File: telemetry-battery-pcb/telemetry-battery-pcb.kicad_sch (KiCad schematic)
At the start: 67 parts, among them J1 Network Connector, J3 CONN_360410_MZC, J5 CONN_360410_MZC, Q1 NMOS, Q2 PMOS, Q4 NMOS, U4 LTC2944, U5 XR76208, U6 M24C02-WMN, U7 TPS1HTC30-Q1

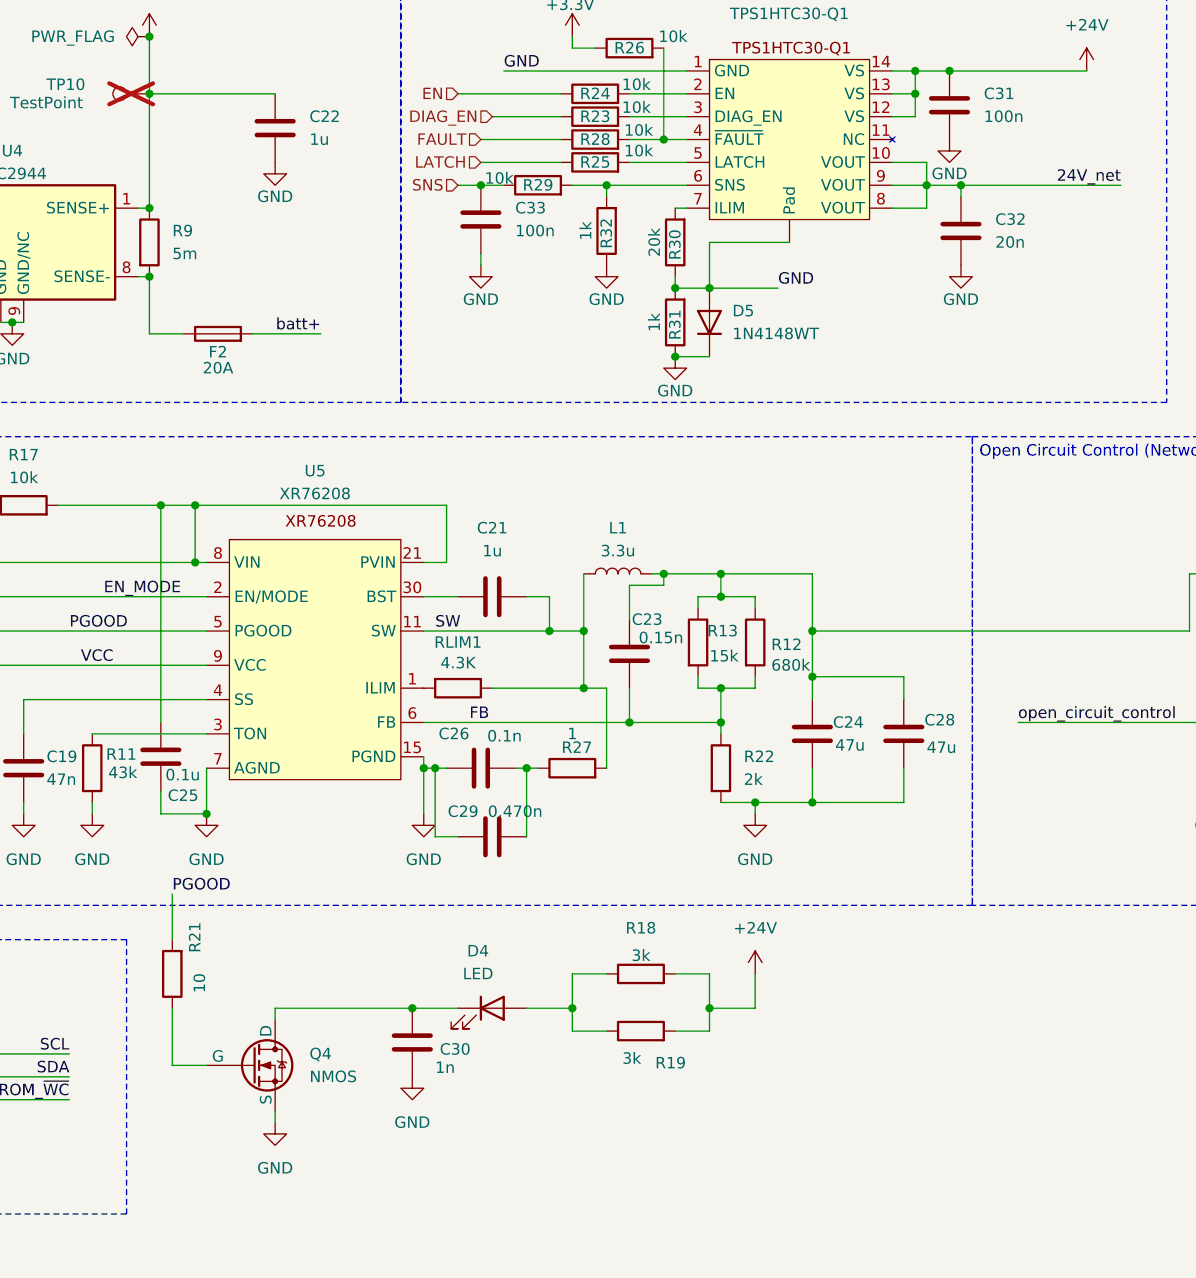
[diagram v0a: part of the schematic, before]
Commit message: telemetry-battery-pcb: schematic connections complete
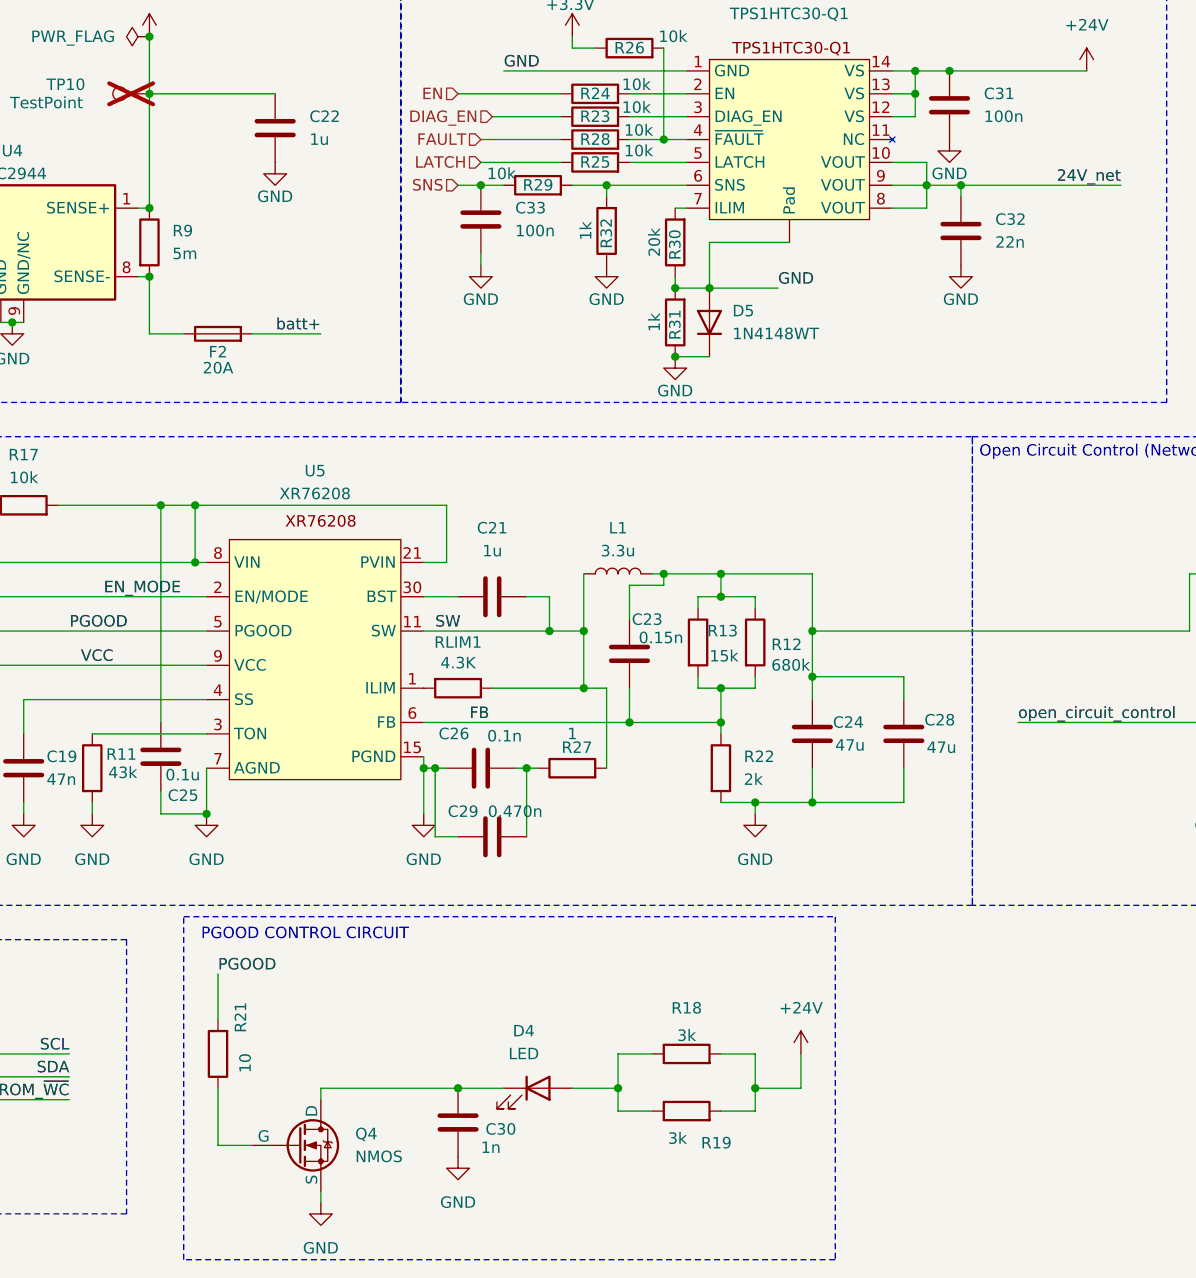
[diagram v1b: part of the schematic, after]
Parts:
- C31, C33: footprint (none) -> Capacitor_SMD:C_0402_1005Metric; JLCPCB (none) -> C1581
- C32: value 20n -> 22n; footprint (none) -> Capacitor_SMD:C_0402_1005Metric; JLCPCB (none) -> C1532
- R23, R24, R25, R26, R28, R29: footprint (none) -> Resistor_SMD:R_0402_1005Metric; JLCPCB (none) -> C25744
- R30: footprint (none) -> Resistor_SMD:R_0201_0603Metric; JLCPCB (none) -> C4184
- R31: footprint (none) -> Resistor_SMD:R_0402_1005Metric; JLCPCB (none) -> C11702
- U5: JLCPCB (none) -> C555356
- U7: footprint (none) -> Package_SO:Texas_HTSSOP-14-1EP_4.4x5mm_P0.65mm_EP3.4x5mm_Mask3.155x3.255mm_ThermalVias; JLCPCB (none) -> C22414694
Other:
- note added: "PGOOD CONTROL CIRCUIT"
- moved on the sheet: C30, D4, Q4, R18, R19, R21

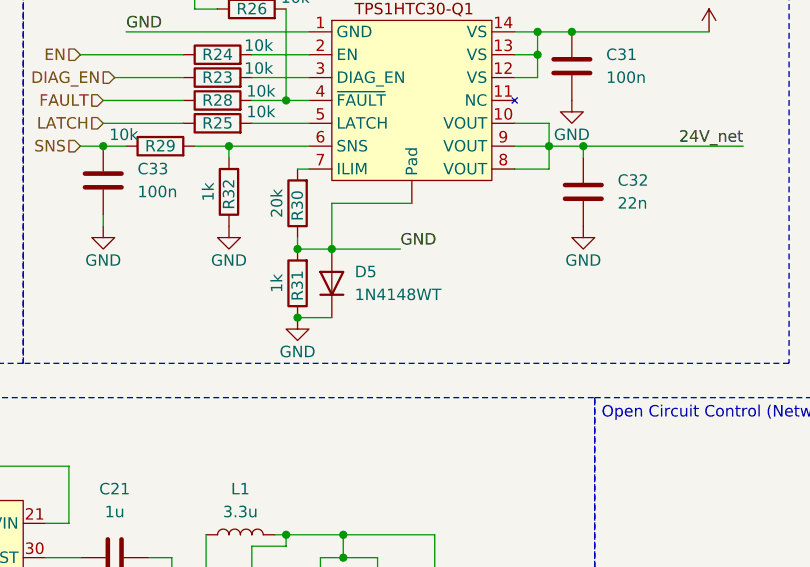
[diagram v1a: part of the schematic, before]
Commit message: telemetry_battery: modify footprint tps1htc30
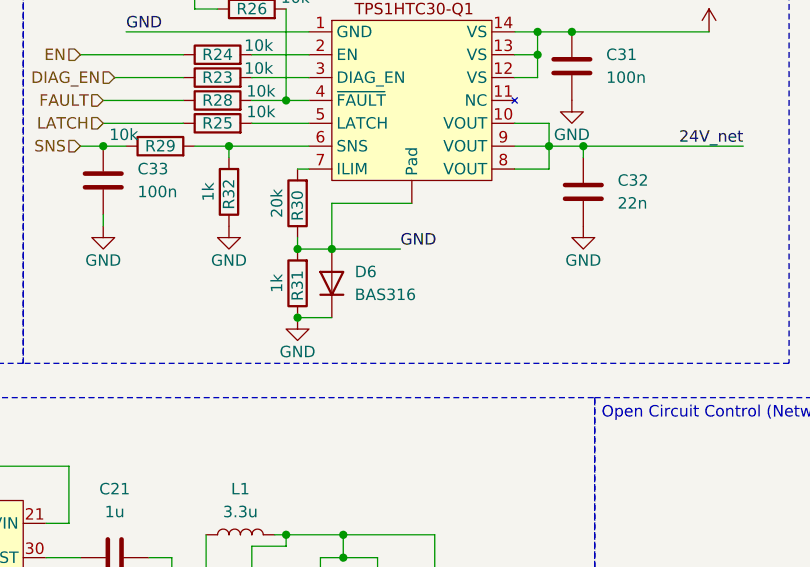
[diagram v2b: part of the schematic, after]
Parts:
- removed D5: 1N4148WT, Diode_SMD:D_SOD-523, symbol Diode:1N4148WT
- added D6: BAS316, Diode_SMD:D_SOD-323, symbol Diode:BAS316
- C31, C33: footprint Capacitor_SMD:C_0402_1005Metric -> Capacitor_SMD:C_0201_0603Metric; JLCPCB C1581 -> C14663
- U7: footprint Package_SO:Texas_HTSSOP-14-1EP_4.4x5mm_P0.65mm_EP3.4x5mm_Mask3.155x3.255mm_ThermalVias -> Exocet:Tps1htc30_Texas_HTSSOP-14-1EP_4.4x5mm_P0.65mm_EP3.4x5mm_Mask3.155x3.255mm_ThermalVias
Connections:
- net GND: now also D6.1 (K), D6.2 (A)
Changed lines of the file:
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@@
 	)
 	(symbol
-		(lib_id "Diode:1N4148WT")
-		(at 130.81 87.63 90)
-		(unit 1)
-		(exclude_from_sim no)
-		(in_bom yes)
-		(on_board yes)
-		(dnp no)
-		(fields_autoplaced yes)
-		(property "Reference" "D5"
-			(at 133.35 86.3599 90)
-			(effects
-				(font
-					(size 1.27 1.27)
-				)
-				(justify right)
-			)
-		)
-		(property "Value" "1N4148WT"
-			(at 133.35 88.8999 90)
-			(effects
-				(font
-					(size 1.27 1.27)
-				)
-				(justify right)
-			)
-		)
-		(property "Footprint" "Diode_SMD:D_SOD-523"
-			(at 135.255 87.63 0)
-			(effects
-				(font
-					(size 1.27 1.27)
-				)
-				(hide yes)
-			)
-		)
-		(property "Datasheet" "https://www.diodes.com/assets/Datasheets/ds30396.pdf"
-			(at 130.81 87.63 0)
-			(effects
-				(font
-					(size 1.27 1.27)
-				)
-				(hide yes)
-			)
-		)
-		(property "Description" "75V 0.15A Fast switching Diode, SOD-523"
-			(at 130.81 87.63 0)
-			(effects
-				(font
-					(size 1.27 1.27)
-				)
-				(hide yes)
-			)
-		)
-		(property "Sim.Device" "D"
-			(at 130.81 87.63 0)
-			(effects
-				(font
-					(size 1.27 1.27)
-				)
-				(hide yes)
-			)
-		)
-		(property "Sim.Pins" "1=K 2=A"
-			(at 130.81 87.63 0)
-			(effects
-				(font
-					(size 1.27 1.27)
-				)
-				(hide yes)
-			)
-		)
-		(pin "2"
-		)
-		(pin "1"
-		)
-		(instances
-			(project ""
-				(path "/4b4cf3aa-c94c-4150-b9c5-35049cd71136"
-					(reference "D5")
-					(unit 1)
-				)
-			)
-		)
-	)
-	(symbol
 		(lib_id "power:GND")
 		(at 158.75 81.28 0)
@@
 	)
 	(symbol
+		(lib_id "Diode:BAS316")
+		(at 130.81 87.63 90)
+		(unit 1)
+		(exclude_from_sim no)
+		(in_bom yes)
+		(on_board yes)
+		(dnp no)
+		(fields_autoplaced yes)
+		(property "Reference" "D6"
+			(at 133.35 86.3599 90)
+			(effects
+				(font
+					(size 1.27 1.27)
+				)
+				(justify right)
+			)
+		)
+		(property "Value" "BAS316"
+			(at 133.35 88.8999 90)
+			(effects
+				(font
+					(size 1.27 1.27)
+				)
+				(justify right)
+			)
+		)
+		(property "Footprint" "Diode_SMD:D_SOD-323"
+			(at 135.255 87.63 0)
+			(effects
+				(font
+					(size 1.27 1.27)
+				)
+				(hide yes)
+			)
+		)
+		(property "Datasheet" "https://assets.nexperia.com/documents/data-sheet/BAS16_SER.pdf"
+			(at 130.81 87.63 0)
+			(effects
+				(font
+					(size 1.27 1.27)
+				)
+				(hide yes)
+			)
+		)
+		(property "Description" "100V, 0.25A, High-speed Switching Diode, SOD-323"
+			(at 130.81 87.63 0)
+			(effects
+				(font
+					(size 1.27 1.27)
+				)
+				(hide yes)
+			)
+		)
+		(property "Sim.Device" "D"
+			(at 130.81 87.63 0)
+			(effects
+				(font
+					(size 1.27 1.27)
+				)
+				(hide yes)
+			)
+		)
+		(property "Sim.Pins" "1=K 2=A"
+			(at 130.81 87.63 0)
+			(effects
+				(font
+					(size 1.27 1.27)
+				)
+				(hide yes)
+			)
+		)
+		(property "JLCPCB" "C2128"
+			(at 130.81 87.63 90)
+			(effects
+				(font
+					(size 1.27 1.27)
+				)
+				(hide yes)
+			)
+		)
+		(pin "1"
+		)
+		(pin "2"
+		)
+		(instances
+			(project ""
+				(path "/4b4cf3aa-c94c-4150-b9c5-35049cd71136"
+					(reference "D6")
+					(unit 1)
+				)
+			)
+		)
+	)
+	(symbol
 		(lib_id "Device:R")
 		(at 118.11 67.31 90)
@@
 			)
 		)
-		(property "Footprint" "Package_SO:Texas_HTSSOP-14-1EP_4.4x5mm_P0.65mm_EP3.4x5mm_Mask3.155x3.255mm_ThermalVias"
+		(property "Footprint" "Exocet:Tps1htc30_Texas_HTSSOP-14-1EP_4.4x5mm_P0.65mm_EP3.4x5mm_Mask3.155x3.255mm_ThermalVias"
 			(at 139.7 53.34 0)
 			(effects
@@
 			)
 		)
-		(property "Datasheet" "https://jlcpcb.com/partdetail/24038323-TPS1HTC30AQPWPRQ1/C22414694"
+		(property "Datasheet" "https://www.ti.com/lit/ds/symlink/tps1htc30-q1.pdf?ts=1772309406015"
 			(at 139.7 53.34 0)
 			(effects
@@
 			)
 		)
-		(property "Footprint" "Capacitor_SMD:C_0402_1005Metric"
+		(property "Footprint" "Capacitor_SMD:C_0201_0603Metric"
 			(at 158.4452 67.31 0)
 			(effects
@@
 			)
 		)
-		(property "JLCPCB" "C1581"
+		(property "JLCPCB" "C14663"
 			(at 157.48 63.5 0)
 			(effects
@@
 			)
 		)
-		(property "Footprint" "Capacitor_SMD:C_0402_1005Metric"
+		(property "Footprint" "Capacitor_SMD:C_0201_0603Metric"
 			(at 106.3752 80.01 0)
 			(effects
@@
 			)
 		)
-		(property "JLCPCB" "C1581"
+		(property "JLCPCB" "C14663"
 			(at 105.41 76.2 0)
 			(effects

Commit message: telemetry battery: move footprint XR76208 to Exocet Library
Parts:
- R32: footprint (none) -> Resistor_SMD:R_0402_1005Metric; JLCPCB (none) -> C11702
- U5: footprint DC-DC_XR76208ELTR-F:MaxLinear_XR76208ELTR-F_QFN-30(5x5) -> Exocet:MaxLinear_XR76208ELTR-F_QFN-30(5x5)
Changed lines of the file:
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@@
 			)
 		)
-		(property "Footprint" ""
+		(property "Footprint" "Resistor_SMD:R_0402_1005Metric"
 			(at 121.158 77.47 90)
 			(effects
@@
 		(property "Description" "Resistor"
 			(at 119.38 77.47 0)
+			(effects
+				(font
+					(size 1.27 1.27)
+				)
+				(hide yes)
+			)
+		)
+		(property "JLCPCB" "C11702"
+			(at 119.38 77.47 90)
 			(effects
 				(font
@@
 			)
 		)
-		(property "Footprint" "DC-DC_XR76208ELTR-F:MaxLinear_XR76208ELTR-F_QFN-30(5x5)"
+		(property "Footprint" "Exocet:MaxLinear_XR76208ELTR-F_QFN-30(5x5)"
 			(at 87.63 105.41 0)
 			(effects

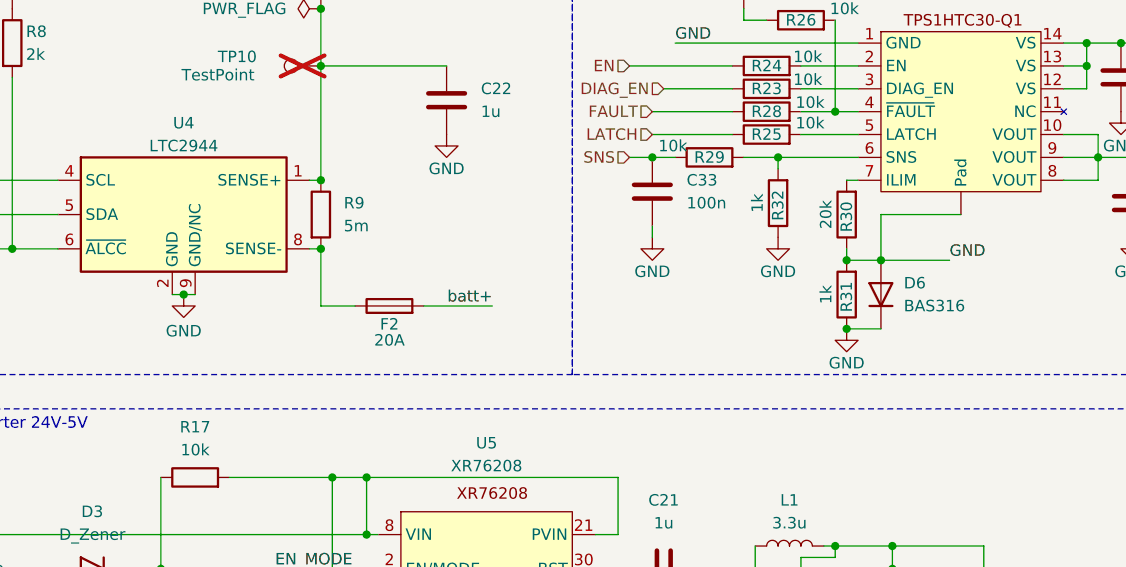
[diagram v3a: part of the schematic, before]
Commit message: telemetry-battery: start of routing
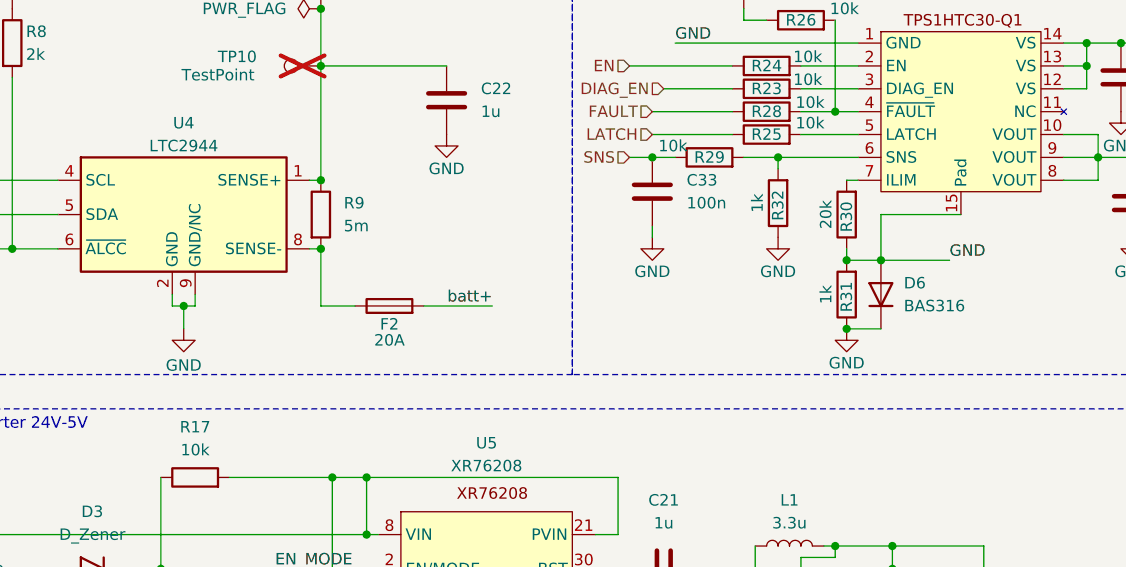
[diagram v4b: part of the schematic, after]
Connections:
- net GND: now also U7.15 (Pad); no longer U7. (Pad)
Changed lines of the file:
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@@
 	)
 	(junction
-		(at 53.34 87.63)
+		(at 53.34 88.9)
 		(diameter 0)
 		(color 0 0 0 0)
@@
 	(wire
 		(pts
-			(xy 52.07 87.63) (xy 53.34 87.63)
+			(xy 52.07 88.9) (xy 53.34 88.9)
 		)
 		(stroke
@@
 	(wire
 		(pts
+			(xy 52.07 88.9) (xy 52.07 87.63)
+		)
+		(stroke
+			(width 0)
+			(type default)
+		)
+	)
+	(wire
+		(pts
 			(xy 115.57 72.39) (xy 119.38 72.39)
 		)
@@
 	(wire
 		(pts
-			(xy 53.34 87.63) (xy 54.61 87.63)
+			(xy 53.34 88.9) (xy 54.61 88.9)
 		)
 		(stroke
@@
 	(wire
 		(pts
+			(xy 54.61 88.9) (xy 54.61 87.63)
+		)
+		(stroke
+			(width 0)
+			(type default)
+		)
+	)
+	(wire
+		(pts
 			(xy 186.69 34.29) (xy 187.96 34.29)
 		)
@@
 	(wire
 		(pts
+			(xy 53.34 91.44) (xy 53.34 88.9)
+		)
+		(stroke
+			(width 0)
+			(type default)
+		)
+	)
+	(wire
+		(pts
 			(xy 73.66 114.3) (xy 74.93 114.3)
 		)
@@
 	(symbol
 		(lib_id "power:GND")
-		(at 53.34 87.63 0)
+		(at 53.34 91.44 0)
 		(unit 1)
 		(exclude_from_sim no)
@@
 		(dnp no)
 		(property "Reference" "#PWR035"
-			(at 53.34 93.98 0)
+			(at 53.34 97.79 0)
 			(effects
 				(font
@@
 		)
 		(property "Value" "GND"
-			(at 53.34 91.694 0)
+			(at 53.34 95.504 0)
 			(effects
 				(font
@@
 		)
 		(property "Footprint" ""
-			(at 53.34 87.63 0)
+			(at 53.34 91.44 0)
 			(effects
 				(font
@@
 		)
 		(property "Datasheet" ""
-			(at 53.34 87.63 0)
+			(at 53.34 91.44 0)
 			(effects
 				(font
@@
 		)
 		(property "Description" "Power symbol creates a global label with name \"GND\" , ground"
-			(at 53.34 87.63 0)
+			(at 53.34 91.44 0)
 			(effects
 				(font
@@
 		(pin "6"
 		)
-		(pin ""
+		(pin "15"
 		)
 		(pin "14"

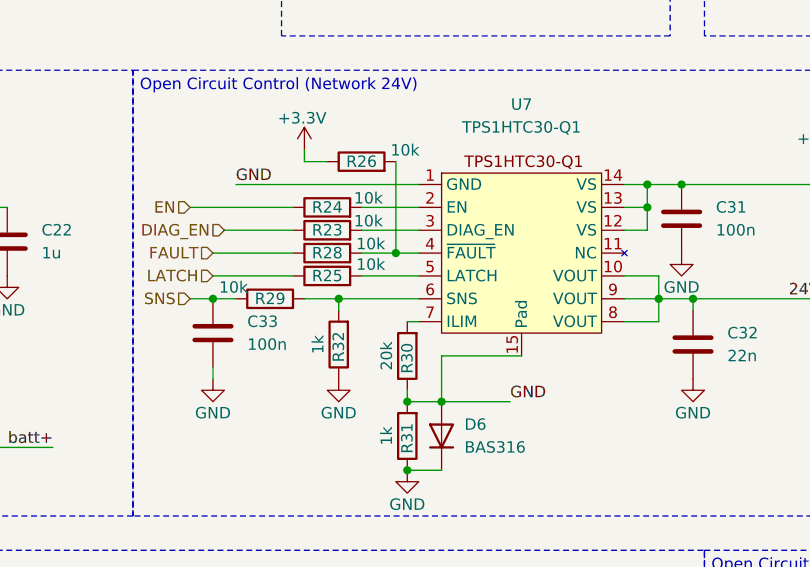
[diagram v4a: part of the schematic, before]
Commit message: telemetry-battery: Placements of parts
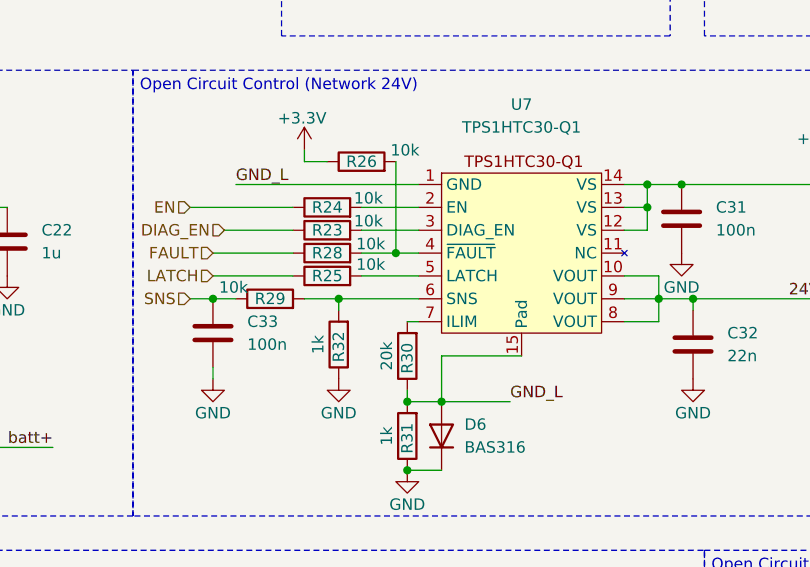
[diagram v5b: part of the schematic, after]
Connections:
- net GND: no longer D6.2 (A), R30.1, R31.2, U7.1 (GND), U7.15 (Pad)
- new net GND_L: D6.2 (A), R30.1, R31.2, U7.1 (GND), U7.15 (Pad)
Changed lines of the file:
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@@
 		)
 	)
-	(label "GND"
+	(label "GND_L"
 		(at 138.43 83.82 0)
 		(effects
@@
 		)
 	)
-	(label "GND"
+	(label "GND_L"
 		(at 107.95 59.69 0)
 		(effects
